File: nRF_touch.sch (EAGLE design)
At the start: 35 parts, among them J1 CORTEX_DEBUG_PTH, T1 BSS84, T2 BC847, U1 ADP160, U2 AT42QT1010-TSHR

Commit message: First routing
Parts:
- added C9: 0.1uF, SparkFun-Capacitors:0.1UF-0603-25V-5%
- added LED1: (no value), adafruit:LEDCHIPLED_1206
- added R12: 330, SparkFun-Resistors:4.7KOHM-0603-1/10W-1%
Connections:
- new net N$1: R12.2, U$1.P024
- new net N$2: LED1.A, R12.1
- net GND: now also C9.2, LED1.C
- net LDO_EN: now also C9.1
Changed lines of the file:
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@@
 <layer number="154" name="FabDoc2" color="2" fill="1" visible="no" active="no"/>
 <layer number="155" name="FabDoc3" color="7" fill="15" visible="no" active="no"/>
-<layer number="199" name="Contour" color="7" fill="1" visible="no" active="yes"/>
+<layer number="199" name="Contour" color="7" fill="1" visible="yes" active="yes"/>
 <layer number="200" name="200bmp" color="1" fill="10" visible="no" active="yes"/>
 <layer number="201" name="201bmp" color="2" fill="1" visible="no" active="no"/>
@@
 <part name="C8" library="SparkFun-Capacitors" deviceset="0.1UF" device="-0603-25V-5%" value="4.7uF"/>
 <part name="SUPPLY15" library="SparkFun-PowerSymbols" deviceset="5V" device=""/>
+<part name="C9" library="SparkFun-Capacitors" deviceset="0.1UF" device="-0603-25V-5%" value="0.1uF"/>
+<part name="GND15" library="SparkFun-PowerSymbols" deviceset="GND" device=""/>
+<part name="LED1" library="adafruit" deviceset="LED" device="CHIPLED_1206"/>
+<part name="GND16" library="SparkFun-PowerSymbols" deviceset="GND" device=""/>
+<part name="R12" library="SparkFun-Resistors" deviceset="4.7KOHM" device="-0603-1/10W-1%" value="330"/>
 </parts>
 <sheets>
@@
 <description>MCU</description>
 <plain>
+<frame x1="-124.46" y1="-40.64" x2="76.2" y2="99.06" columns="8" rows="5" layer="91"/>
+<wire x1="-119.38" y1="45.72" x2="-66.04" y2="45.72" width="1.016" layer="199"/>
+<wire x1="-66.04" y1="45.72" x2="-40.64" y2="45.72" width="1.016" layer="199"/>
+<wire x1="-40.64" y1="45.72" x2="71.12" y2="45.72" width="1.016" layer="199"/>
+<wire x1="-40.64" y1="45.72" x2="-40.64" y2="93.98" width="1.016" layer="199"/>
+<wire x1="-66.04" y1="45.72" x2="-66.04" y2="-35.56" width="1.016" layer="199"/>
 </plain>
 <instances>
@@
 <instance part="GND6" gate="1" x="7.62" y="35.56" rot="R180"/>
 <instance part="J2" gate="G$1" x="-99.06" y="5.08"/>
+<instance part="LED1" gate="G$1" x="53.34" y="0" rot="R90"/>
+<instance part="GND16" gate="1" x="66.04" y="0" rot="R90"/>
+<instance part="R12" gate="G$1" x="40.64" y="0" rot="R180"/>
 </instances>
 <busses>
@@
 <label x="-88.9" y="2.54" size="0.762" layer="95" xref="yes"/>
 </segment>
+<segment>
+<pinref part="LED1" gate="G$1" pin="C"/>
+<pinref part="GND16" gate="1" pin="GND"/>
+<wire x1="58.42" y1="0" x2="63.5" y2="0" width="0.1524" layer="91"/>
+</segment>
 </net>
 <net name="SHARP_CS" class="0">
@@
 <wire x1="27.94" y1="7.62" x2="35.56" y2="7.62" width="0.1524" layer="91"/>
 <label x="35.56" y="7.62" size="0.762" layer="95" xref="yes"/>
+</segment>
+</net>
+<net name="N$1" class="1">
+<segment>
+<pinref part="U$1" gate="G$1" pin="P024"/>
+<pinref part="R12" gate="G$1" pin="2"/>
+<wire x1="27.94" y1="0" x2="35.56" y2="0" width="0.1524" layer="91"/>
+</segment>
+</net>
+<net name="N$2" class="1">
+<segment>
+<pinref part="R12" gate="G$1" pin="1"/>
+<pinref part="LED1" gate="G$1" pin="A"/>
+<wire x1="45.72" y1="0" x2="50.8" y2="0" width="0.1524" layer="91"/>
 </segment>
 </net>
@@
 <description>PERIPH</description>
 <plain>
+<frame x1="-71.12" y1="-45.72" x2="205.74" y2="88.9" columns="8" rows="5" layer="91"/>
+<wire x1="58.42" y1="83.82" x2="58.42" y2="60.96" width="1.016" layer="199"/>
+<wire x1="58.42" y1="60.96" x2="58.42" y2="35.56" width="1.016" layer="199"/>
+<wire x1="58.42" y1="35.56" x2="58.42" y2="15.24" width="1.016" layer="199"/>
+<wire x1="58.42" y1="15.24" x2="58.42" y2="2.54" width="1.016" layer="199"/>
+<wire x1="58.42" y1="2.54" x2="58.42" y2="-40.64" width="1.016" layer="199"/>
+<wire x1="58.42" y1="15.24" x2="200.66" y2="15.24" width="1.016" layer="199"/>
+<wire x1="58.42" y1="60.96" x2="-66.04" y2="60.96" width="1.016" layer="199"/>
+<wire x1="58.42" y1="35.56" x2="-66.04" y2="35.56" width="1.016" layer="199"/>
+<wire x1="58.42" y1="2.54" x2="-66.04" y2="2.54" width="1.016" layer="199"/>
 </plain>
 <instances>
@@
 <description>Power</description>
 <plain>
+<frame x1="-114.3" y1="-38.1" x2="101.6" y2="73.66" columns="8" rows="5" layer="91"/>
+<wire x1="0" y1="68.58" x2="0" y2="17.78" width="1.016" layer="199"/>
+<wire x1="0" y1="17.78" x2="0" y2="2.54" width="1.016" layer="199"/>
+<wire x1="0" y1="2.54" x2="0" y2="-33.02" width="1.016" layer="199"/>
+<wire x1="0" y1="2.54" x2="96.52" y2="2.54" width="1.016" layer="199"/>
+<wire x1="0" y1="17.78" x2="-109.22" y2="17.78" width="1.016" layer="199"/>
 </plain>
 <instances>
@@
 <instance part="C8" gate="G$1" x="-81.28" y="-17.78"/>
 <instance part="SUPPLY15" gate="G$1" x="-81.28" y="-5.08"/>
+<instance part="C9" gate="G$1" x="60.96" y="58.42"/>
+<instance part="GND15" gate="1" x="60.96" y="50.8"/>
 </instances>
 <busses>
@@
 <junction x="-88.9" y="43.18"/>
 </segment>
+<segment>
+<pinref part="GND15" gate="1" pin="GND"/>
+<pinref part="C9" gate="G$1" pin="2"/>
+<wire x1="60.96" y1="53.34" x2="60.96" y2="55.88" width="0.1524" layer="91"/>
+</segment>
 </net>
 <net name="VCC" class="1">
@@
 <segment>
 <pinref part="T1" gate="G$1" pin="D"/>
-<wire x1="45.72" y1="66.04" x2="76.2" y2="66.04" width="0.1524" layer="91"/>
+<wire x1="45.72" y1="66.04" x2="60.96" y2="66.04" width="0.1524" layer="91"/>
 <label x="76.2" y="66.04" size="1.778" layer="95" xref="yes"/>
-</segment>
-</net>
+<pinref part="C9" gate="G$1" pin="1"/>
+<wire x1="60.96" y1="66.04" x2="76.2" y2="66.04" width="0.1524" layer="91"/>
+<wire x1="60.96" y1="63.5" x2="60.96" y2="66.04" width="0.1524" layer="91"/>
+<junction x="60.96" y="66.04"/>
+</segment>
+</net>

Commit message: Improvements #1
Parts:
- added C10: 0.1uF, SparkFun-Capacitors:0.1UF-0603-25V-5%
- U$4: value SHARP27_REV -> SHARP27; device sharp:SHARP27_REV -> sharp:SHARP27
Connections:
- net 5V: now also C10.2
- net GND: now also C10.1
- net VCC: now also U$4.VDDA
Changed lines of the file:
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@@
 <clearance class="1" value="0.254"/>
+</class>
+<class number="2" name="touch" width="0.1524" drill="0.254">
+<clearance class="2" value="0.3556"/>
 </class>
 </classes>
@@
 <part name="SUPPLY9" library="SparkFun-PowerSymbols" deviceset="VCC" device=""/>
 <part name="GND6" library="SparkFun-PowerSymbols" deviceset="GND" device=""/>
-<part name="U$4" library="sharp" deviceset="SHARP27_REV" device=""/>
 <part name="SUPPLY10" library="SparkFun-PowerSymbols" deviceset="VCC" device=""/>
 <part name="GND7" library="SparkFun-PowerSymbols" deviceset="GND" device=""/>
@@
 <part name="GND16" library="SparkFun-PowerSymbols" deviceset="GND" device=""/>
 <part name="R12" library="SparkFun-Resistors" deviceset="4.7KOHM" device="-0603-1/10W-1%" value="330"/>
+<part name="C10" library="SparkFun-Capacitors" deviceset="0.1UF" device="-0603-25V-5%" value="0.1uF"/>
+<part name="GND17" library="SparkFun-PowerSymbols" deviceset="GND" device=""/>
+<part name="U$4" library="sharp" deviceset="SHARP27" device=""/>
 </parts>
 <sheets>
@@
 </busses>
 <nets>
-<net name="AIN2" class="0">
+<net name="AIN2" class="2">
 <segment>
 <pinref part="U$1" gate="G$1" pin="P001/AIN2"/>
@@
 </segment>
 </net>
-<net name="AIN3" class="0">
+<net name="AIN3" class="2">
 <segment>
 <pinref part="U$1" gate="G$1" pin="P002/AIN3"/>
@@
 </segment>
 </net>
-<net name="AIN4" class="0">
+<net name="AIN4" class="2">
 <segment>
 <pinref part="U$1" gate="G$1" pin="P003/AIN4"/>
@@
 </segment>
 </net>
-<net name="AIN5" class="0">
+<net name="AIN5" class="2">
 <segment>
 <pinref part="U$1" gate="G$1" pin="P004/AIN5"/>
@@
 <instance part="SUPPLY4" gate="G$1" x="180.34" y="-15.24" rot="R270"/>
 <instance part="SUPPLY5" gate="G$1" x="83.82" y="-20.32" rot="R90"/>
-<instance part="U$4" gate="A" x="-17.78" y="-30.48"/>
 <instance part="SUPPLY10" gate="G$1" x="35.56" y="-12.7" rot="R270"/>
 <instance part="GND7" gate="1" x="38.1" y="-27.94" rot="R90"/>
@@
 <instance part="S2" gate="G$1" x="88.9" y="40.64" rot="MR90"/>
 <instance part="GND14" gate="1" x="73.66" y="38.1" rot="R270"/>
+<instance part="U$4" gate="G$1" x="-17.78" y="-30.48"/>
 </instances>
 <busses>
@@
 </segment>
 </net>
-<net name="AIN2" class="0">
+<net name="AIN2" class="2">
 <segment>
 <pinref part="S1" gate="G$1" pin="P$1"/>
@@
 </segment>
 </net>
-<net name="AIN3" class="0">
+<net name="AIN3" class="2">
 <segment>
 <pinref part="S1" gate="G$1" pin="P$2"/>
@@
 </segment>
 </net>
-<net name="AIN4" class="0">
+<net name="AIN4" class="2">
 <segment>
 <pinref part="S1" gate="G$1" pin="P$3"/>
@@
 </segment>
 </net>
-<net name="AIN5" class="0">
+<net name="AIN5" class="2">
 <segment>
 <pinref part="S1" gate="G$1" pin="P$4"/>
@@
 </segment>
 <segment>
-<pinref part="U$4" gate="A" pin="VSS"/>
 <wire x1="20.32" y1="-22.86" x2="27.94" y2="-22.86" width="0.1524" layer="91"/>
 <wire x1="27.94" y1="-22.86" x2="27.94" y2="-27.94" width="0.1524" layer="91"/>
 <pinref part="GND7" gate="1" pin="GND"/>
 <wire x1="27.94" y1="-27.94" x2="35.56" y2="-27.94" width="0.1524" layer="91"/>
-<pinref part="U$4" gate="A" pin="VSSA"/>
 <wire x1="20.32" y1="-27.94" x2="27.94" y2="-27.94" width="0.1524" layer="91"/>
 <junction x="27.94" y="-27.94"/>
+<pinref part="U$4" gate="G$1" pin="VSS"/>
+<pinref part="U$4" gate="G$1" pin="VSSA"/>
 </segment>
 <segment>
@@
 </segment>
 <segment>
-<pinref part="U$4" gate="A" pin="VDD"/>
 <pinref part="SUPPLY10" gate="G$1" pin="VCC"/>
-<wire x1="20.32" y1="-12.7" x2="35.56" y2="-12.7" width="0.1524" layer="91"/>
+<wire x1="20.32" y1="-12.7" x2="27.94" y2="-12.7" width="0.1524" layer="91"/>
+<pinref part="U$4" gate="G$1" pin="VDD"/>
+<pinref part="U$4" gate="G$1" pin="VDDA"/>
+<wire x1="27.94" y1="-12.7" x2="35.56" y2="-12.7" width="0.1524" layer="91"/>
+<wire x1="20.32" y1="-7.62" x2="27.94" y2="-7.62" width="0.1524" layer="91"/>
+<wire x1="27.94" y1="-7.62" x2="27.94" y2="-12.7" width="0.1524" layer="91"/>
+<junction x="27.94" y="-12.7"/>
 </segment>
 <segment>
@@
 </segment>
 <segment>
-<pinref part="U$4" gate="A" pin="MOSI"/>
 <wire x1="-22.86" y1="-12.7" x2="-45.72" y2="-12.7" width="0.1524" layer="91"/>
 <label x="-45.72" y="-12.7" size="1.778" layer="95" rot="R180" xref="yes"/>
+<pinref part="U$4" gate="G$1" pin="MOSI"/>
 </segment>
 </net>
@@
 </segment>
 <segment>
-<pinref part="U$4" gate="A" pin="SCLK"/>
 <wire x1="-22.86" y1="-7.62" x2="-33.02" y2="-7.62" width="0.1524" layer="91"/>
 <label x="-33.02" y="-7.62" size="1.778" layer="95" rot="R180" xref="yes"/>
+<pinref part="U$4" gate="G$1" pin="SCLK"/>
 </segment>
 </net>
@@
 <net name="SHARP_CS" class="0">
 <segment>
-<pinref part="U$4" gate="A" pin="CS"/>
 <wire x1="-22.86" y1="-17.78" x2="-33.02" y2="-17.78" width="0.1524" layer="91"/>
 <label x="-33.02" y="-17.78" size="1.778" layer="95" rot="R180" xref="yes"/>
+<pinref part="U$4" gate="G$1" pin="CS"/>
 </segment>
 </net>
@@
 <segment>
 <pinref part="R6" gate="G$1" pin="2"/>
-<pinref part="U$4" gate="A" pin="EXTCOMM"/>
 <wire x1="-30.48" y1="-22.86" x2="-22.86" y2="-22.86" width="0.1524" layer="91"/>
+<pinref part="U$4" gate="G$1" pin="EXTCOMM"/>
 </segment>
 </net>
 <net name="EXTMODE" class="0">
 <segment>
-<pinref part="U$4" gate="A" pin="EXTMODE"/>
 <pinref part="R5" gate="G$1" pin="1"/>
 <wire x1="20.32" y1="-17.78" x2="25.4" y2="-17.78" width="0.1524" layer="91"/>
+<pinref part="U$4" gate="G$1" pin="EXTMODE"/>
 </segment>
 </net>
@@
 <segment>
 <pinref part="C1" gate="G$1" pin="2"/>
-<pinref part="U$4" gate="A" pin="DISP"/>
 <wire x1="-25.4" y1="-27.94" x2="-22.86" y2="-27.94" width="0.1524" layer="91"/>
 <pinref part="R7" gate="G$1" pin="2"/>
 <wire x1="-33.02" y1="-33.02" x2="-22.86" y2="-33.02" width="0.1524" layer="91"/>
 <wire x1="-22.86" y1="-33.02" x2="-22.86" y2="-27.94" width="0.1524" layer="91"/>
+<pinref part="U$4" gate="G$1" pin="DISP"/>
 <junction x="-22.86" y="-27.94"/>
 </segment>
 </net>
-<net name="PAD" class="0">
+<net name="PAD" class="2">
 <segment>
 <pinref part="S2" gate="G$1" pin="P$1"/>
@@
 <instance part="C9" gate="G$1" x="60.96" y="58.42"/>
 <instance part="GND15" gate="1" x="60.96" y="50.8"/>
+<instance part="C10" gate="G$1" x="-88.9" y="58.42"/>
+<instance part="GND17" gate="1" x="-88.9" y="68.58" rot="R180"/>
 </instances>
 <busses>
@@
 <segment>
 <pinref part="U2" gate="A" pin="VDD"/>
-<wire x1="-81.28" y1="53.34" x2="-96.52" y2="53.34" width="0.1524" layer="91"/>
+<wire x1="-81.28" y1="53.34" x2="-88.9" y2="53.34" width="0.1524" layer="91"/>
 <label x="-96.52" y="53.34" size="1.778" layer="95" rot="R180" xref="yes"/>
+<pinref part="C10" gate="G$1" pin="2"/>
+<wire x1="-88.9" y1="53.34" x2="-96.52" y2="53.34" width="0.1524" layer="91"/>
+<wire x1="-88.9" y1="55.88" x2="-88.9" y2="53.34" width="0.1524" layer="91"/>
+<junction x="-88.9" y="53.34"/>
 </segment>
 <segment>
@@
 <wire x1="60.96" y1="53.34" x2="60.96" y2="55.88" width="0.1524" layer="91"/>
 </segment>
+<segment>
+<pinref part="GND17" gate="1" pin="GND"/>
+<pinref part="C10" gate="G$1" pin="1"/>
+<wire x1="-88.9" y1="66.04" x2="-88.9" y2="63.5" width="0.1524" layer="91"/>
+</segment>
 </net>
 <net name="VCC" class="1">
@@
 </segment>
 </net>
-<net name="PAD" class="0">
+<net name="PAD" class="2">
 <segment>
 <pinref part="R11" gate="G$1" pin="1"/>

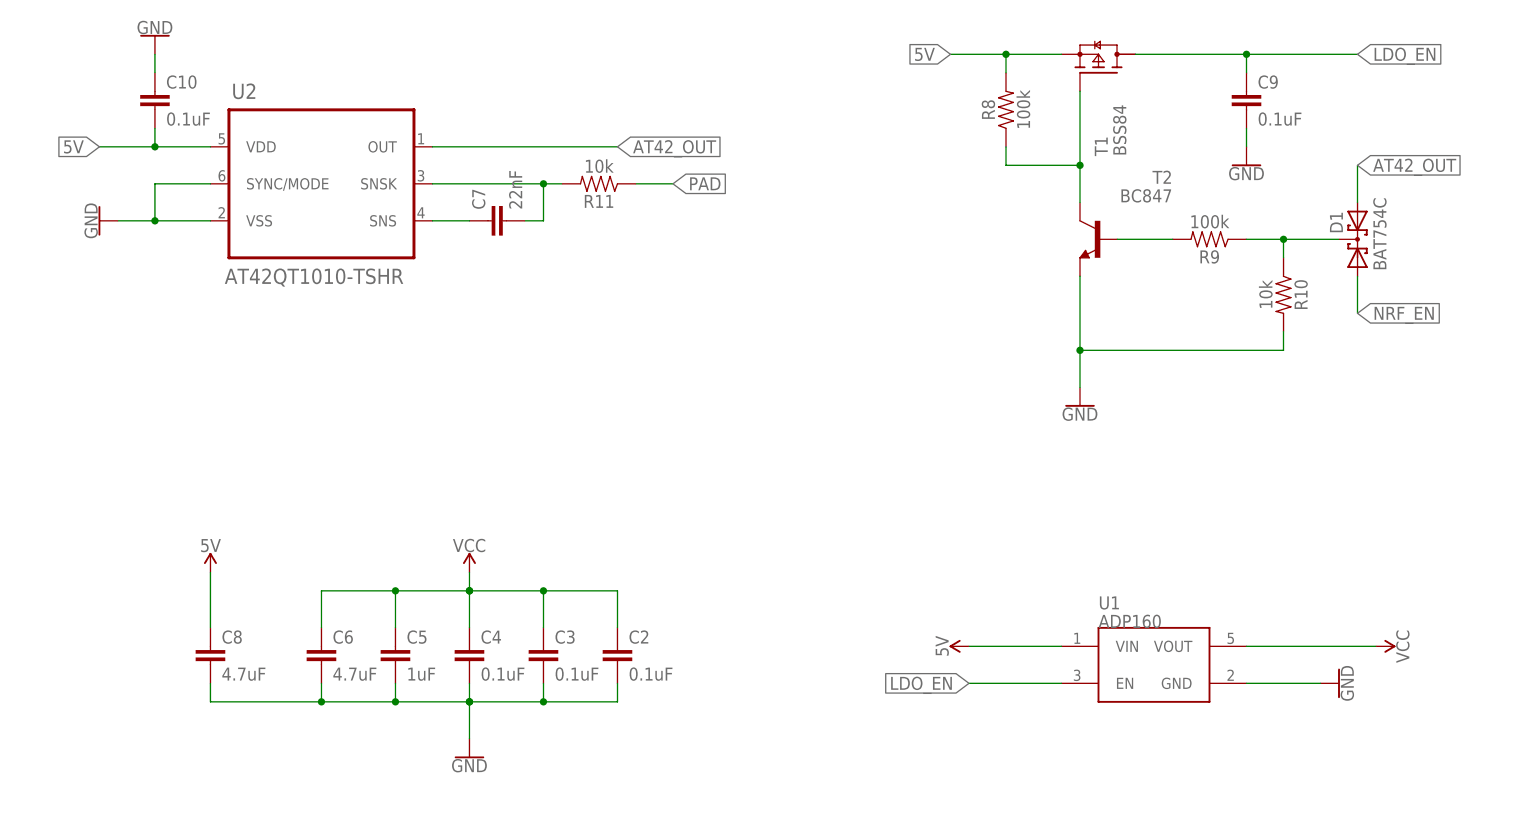
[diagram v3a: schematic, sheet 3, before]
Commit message: Addition of neopixel and change in logic
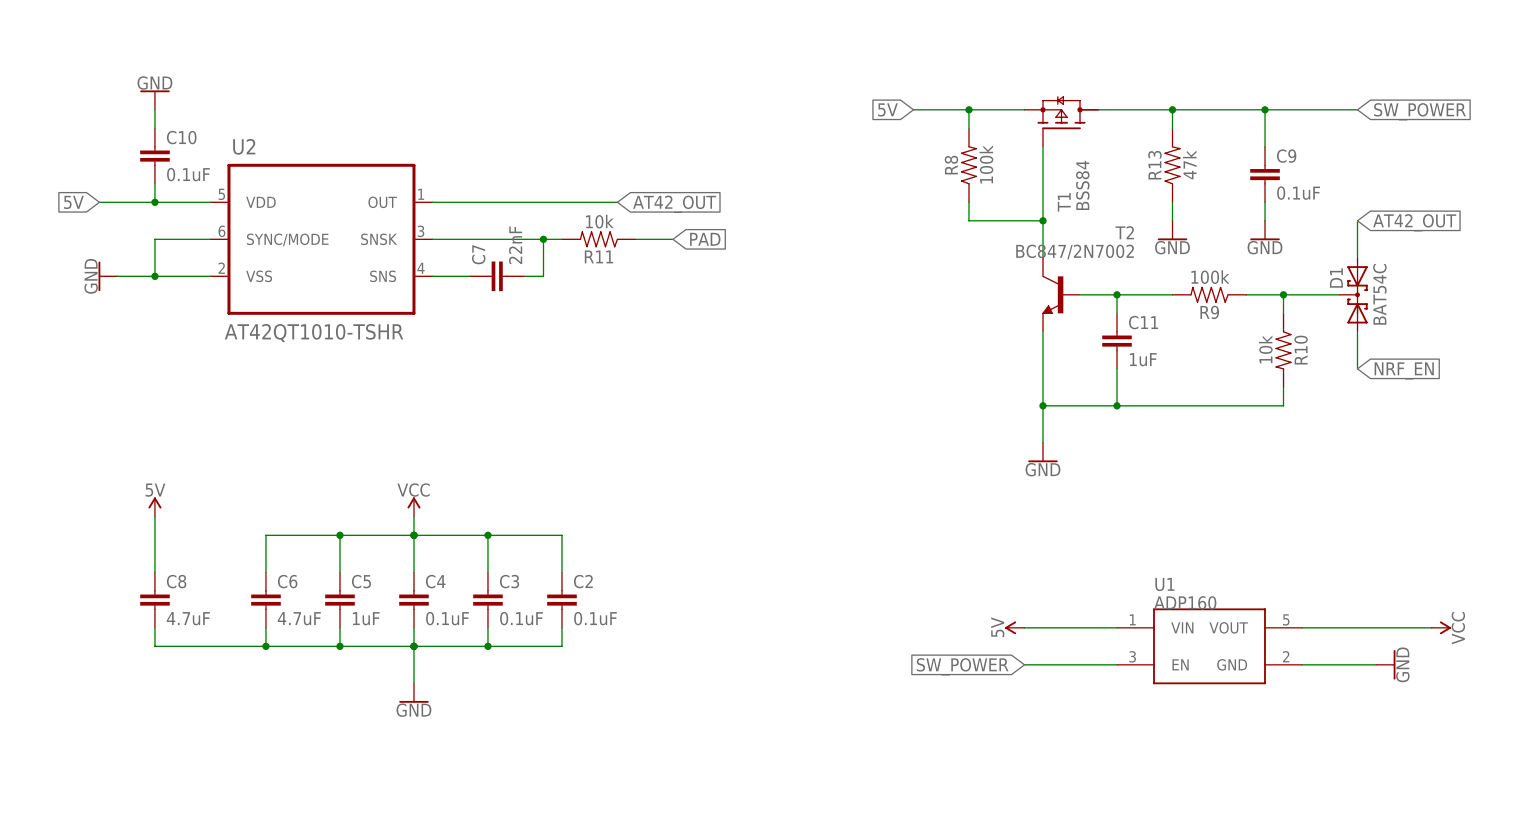
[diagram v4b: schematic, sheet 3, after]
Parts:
- removed J1: CORTEX_DEBUG_PTH, SparkFun-Connectors:CORTEX_DEBUG_PTH
- removed JP1: (no value), SparkFun-Retired:JUMPER-2SMD-NC
- added C11: 1uF, SparkFun-Capacitors:0.1UF-0603-25V-5%
- added J3: (no value), SparkFun-Connectors:CONN_03
- added L1: WS2812B, adafruit:WS2812B
- added Q1: BSS138BKW, BSS138:BSS138BKW
- added R13: 47k, SparkFun-Resistors:4.7KOHM-0603-1/10W-1%
- added R14, R15: 10k, SparkFun-Resistors:4.7KOHM-0603-1/10W-1%
- added S3: L_BUTTON, qtouch:BUTTON
- added U3: (no value), adafruit:GPS_FGPMMOPA6H
- D1: value BAT754C -> BAT54C
- J2: device SparkFun-Connectors:CONN_06NO_SILK_FEMALE_PTH -> SparkFun-Connectors:CONN_09
- S1: value SLIDER -> L_BUTTON; device qtouch:SLIDER -> qtouch:BUTTON
- T2: value BC847 -> BC847/2N7002
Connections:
- removed net AIN2: S1.P$1, U$1.P001/AIN2
- removed net AIN4: S1.P$3, U$1.P003/AIN4
- removed net LDO_EN: C9.1, T1.D, U1.EN
- removed net N$10: JP1.1, S1.GND
- new net NEO_DIN: L1.DIN, Q1.D, R14.1
- new net NEO_PIN: Q1.S, R15.1, U$1.P008
- new net SW_POWER: C9.1, L1.VDD, R13.2, R14.2, T1.D, U1.EN
- net AIN3: now also S3.P$1; no longer S1.P$2
- net AIN5: now also S1.P$1; no longer S1.P$4
- net GND: now also C11.2, L1.GND, R13.1, S1.GND, S3.GND; no longer J1.GND@3, J1.GND@5, J1.GNDDTCT, JP1.2
- net N$11: now also C11.1
- net SHARP_CS: no longer U$1.P008
- net SPIS_MI: no longer U$1.P018
- net SPIS_MO: no longer U$1.P016
- net SPIS_SCK: no longer U$1.P019
- net SST_CS: now also J2.7; no longer U$1.P013
- net SWDCLK: now also J3.2; no longer J1.SWDCLK/TCK
- net SWDIO: now also J3.1; no longer J1.SWDIO/TMS
- net VCC: now also J2.9, J3.3, Q1.G, R15.2; no longer J1.VCC
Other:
- moved on the sheet: C10, C2, C3, C4, C5, C6, C7, C8, C9, D1, R10, R11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
